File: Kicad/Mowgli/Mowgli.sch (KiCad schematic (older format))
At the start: 1 part

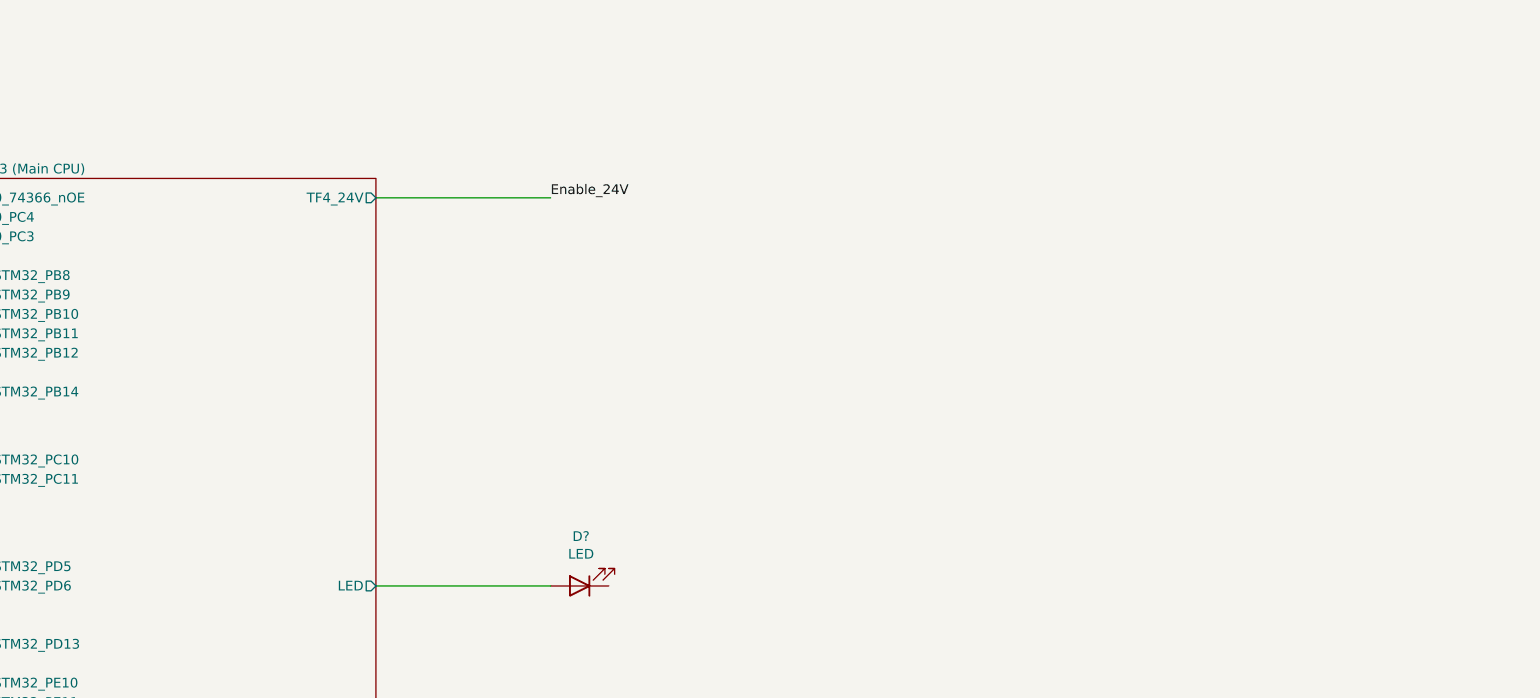
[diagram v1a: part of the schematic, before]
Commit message: updated Kicad with Charge/Battery Circuit
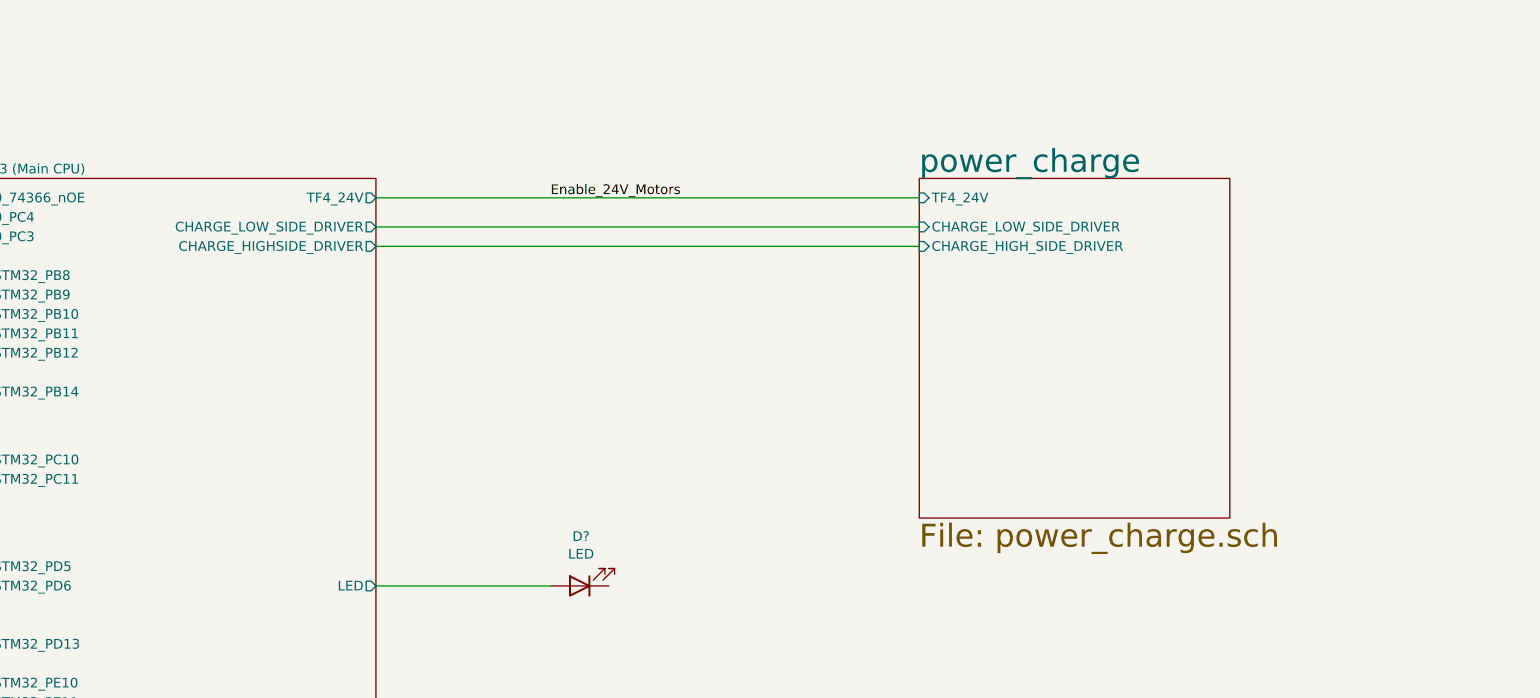
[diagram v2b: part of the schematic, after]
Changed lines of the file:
@@
 $Descr A3 16535 11693
 encoding utf-8
-Sheet 1 9
+Sheet 1 10
 Title "Project Mowgli"
 Date "2022-05-22"
@@
 F29 "ACCEL_SCL" O R 9500 6950 50
 F30 "ACCEL_SDA" O R 9500 7050 50
+F31 "CHARGE_LOW_SIDE_DRIVER" O R 9500 3100 50
+F32 "CHARGE_HIGHSIDE_DRIVER" O R 9500 3200 50
 $EndSheet
 Wire Wire Line
@@
 USART 3
 Text Label 10400 2950 0    50   ~ 0
-Enable_24V
-Wire Wire Line
-	9500 2950 10400 2950
+Enable_24V_Motors
 $Sheet
 S 5550 6950 850  1350
@@
 F30 "J18_Pin_8" I L 4200 6000 50
 $EndSheet
+$Sheet
+S 12300 2850 1600 1750
+U 628DB6FB
+F0 "power_charge" 118
+F1 "power_charge.sch" 118
+F2 "TF4_24V" I L 12300 2950 50
+F3 "CHARGE_LOW_SIDE_DRIVER" I L 12300 3100 50
+F4 "CHARGE_HIGH_SIDE_DRIVER" I L 12300 3200 50
+$EndSheet
+Wire Wire Line
+	9500 2950 12300 2950
+Wire Wire Line
+	12300 3100 9500 3100
+Wire Wire Line
+	9500 3200 12300 3200
 Wire Bus Line
 	6450 8750 6450 9050

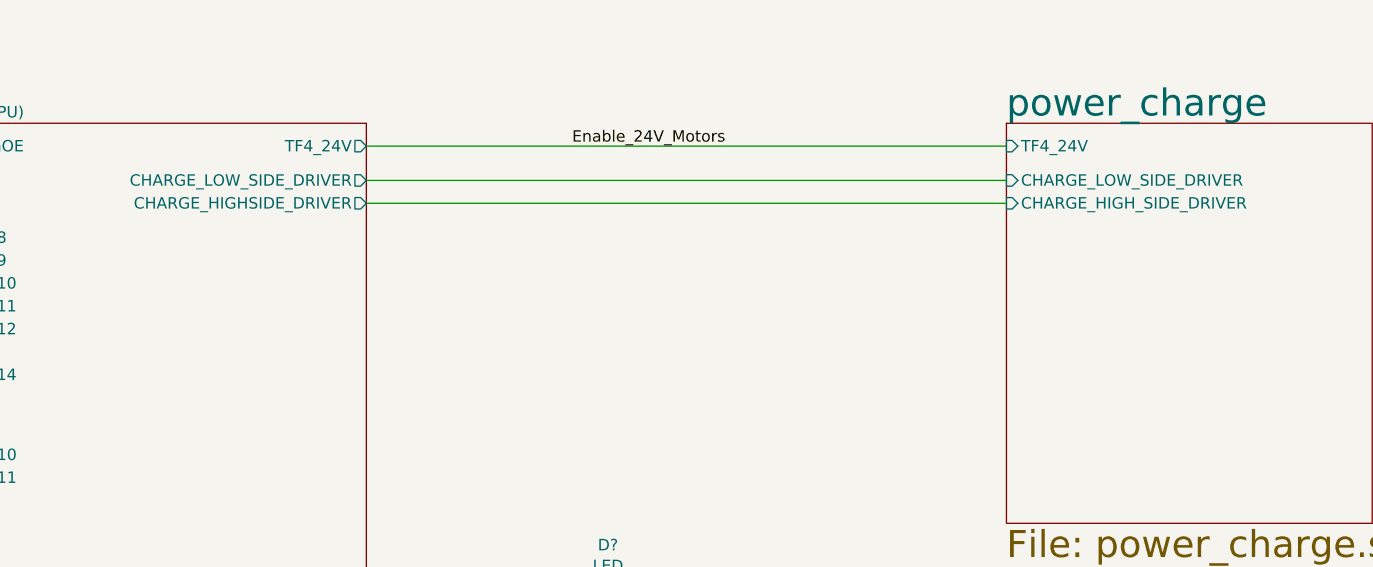
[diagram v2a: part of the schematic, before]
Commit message: added PA3 ADC input pin
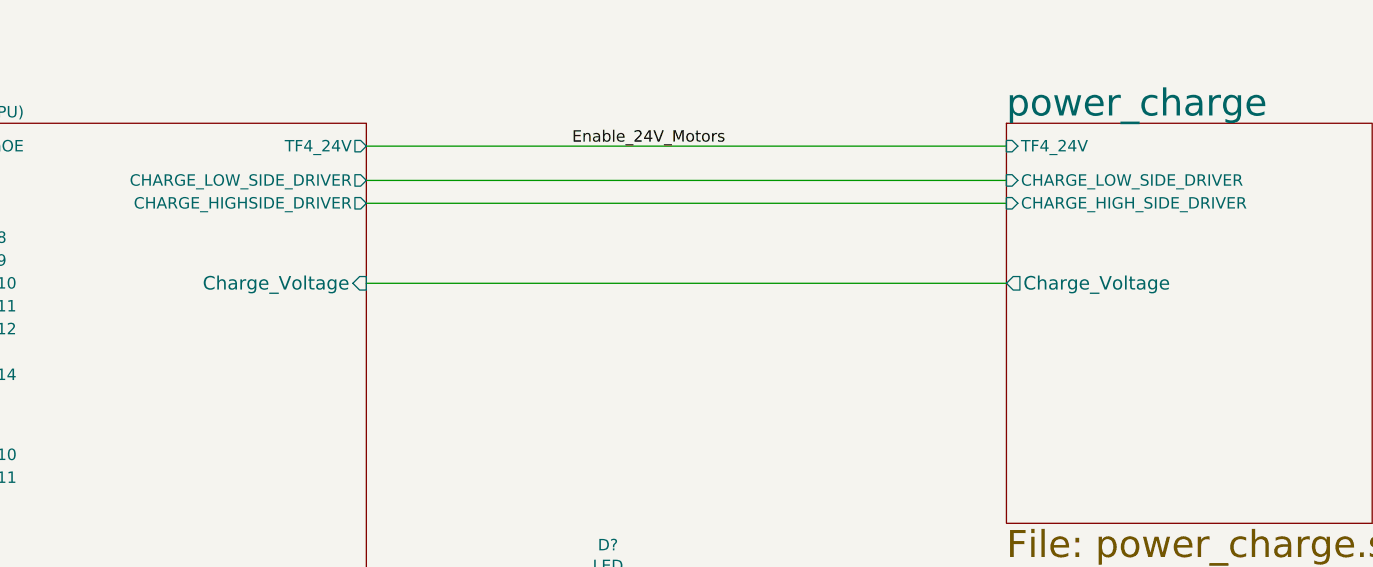
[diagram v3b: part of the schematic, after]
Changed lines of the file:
@@
 F31 "CHARGE_LOW_SIDE_DRIVER" O R 9500 3100 50
 F32 "CHARGE_HIGHSIDE_DRIVER" O R 9500 3200 50
+F33 "Charge_Voltage" I R 9500 3550 59
 $EndSheet
 Wire Wire Line
@@
 F3 "CHARGE_LOW_SIDE_DRIVER" I L 12300 3100 50
 F4 "CHARGE_HIGH_SIDE_DRIVER" I L 12300 3200 50
+F5 "Charge_Voltage" O L 12300 3550 59
 $EndSheet
 Wire Wire Line
@@
 Wire Wire Line
 	9500 3200 12300 3200
+Wire Wire Line
+	12300 3550 9500 3550
 Wire Bus Line
 	6450 8750 6450 9050

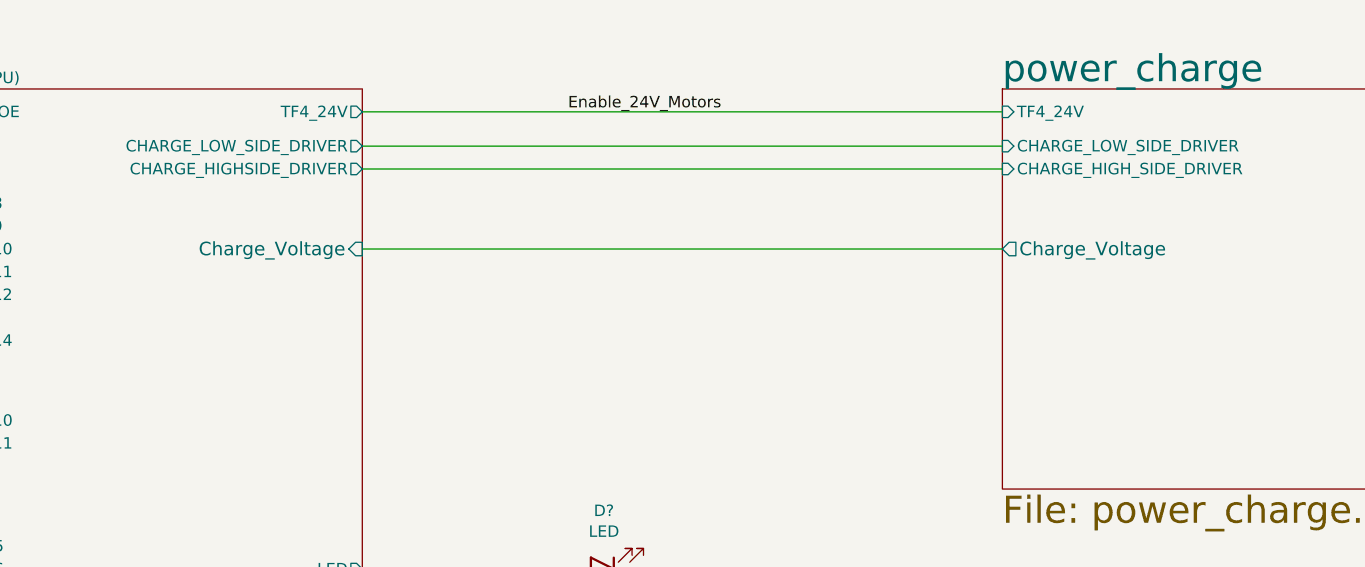
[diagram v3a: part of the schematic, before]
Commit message: PA2,PA3 are used for Charging and Battery Voltage monitoring - added stm32 code and updated KiCad
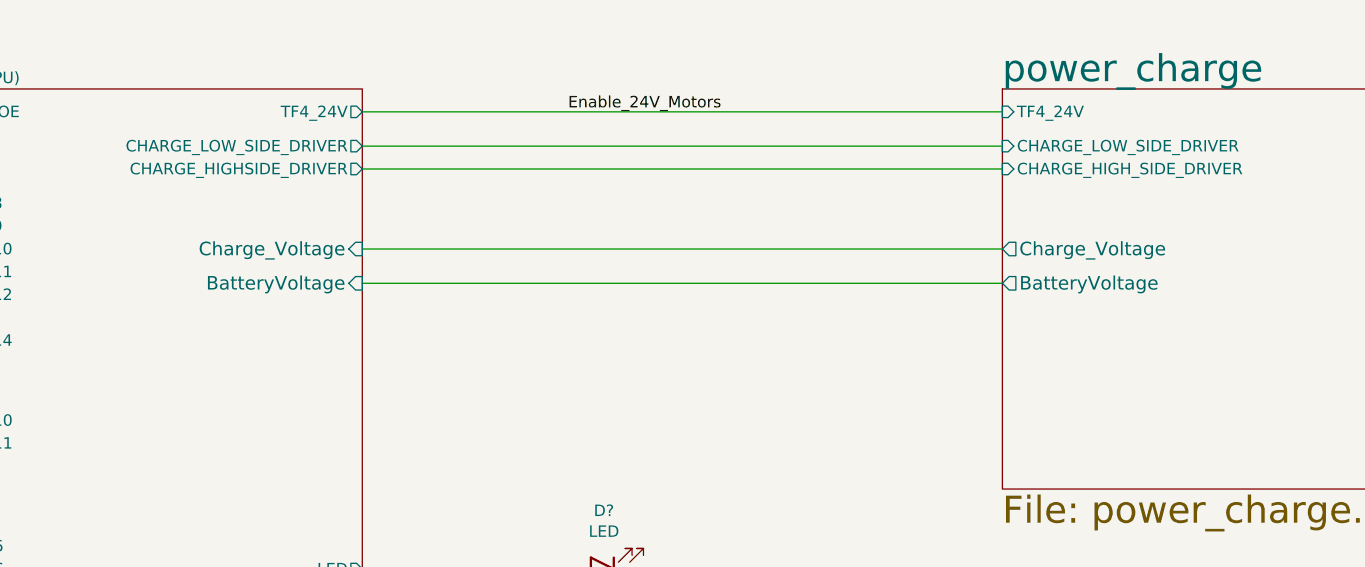
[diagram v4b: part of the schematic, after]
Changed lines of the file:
@@
 F32 "CHARGE_HIGHSIDE_DRIVER" O R 9500 3200 50
 F33 "Charge_Voltage" I R 9500 3550 59
+F34 "BatteryVoltage" I R 9500 3700 59
 $EndSheet
 Wire Wire Line
@@
 F4 "CHARGE_HIGH_SIDE_DRIVER" I L 12300 3200 50
 F5 "Charge_Voltage" O L 12300 3550 59
+F6 "BatteryVoltage" O L 12300 3700 59
 $EndSheet
 Wire Wire Line
@@
 Wire Wire Line
 	12300 3550 9500 3550
+Wire Wire Line
+	12300 3700 9500 3700
 Wire Bus Line
 	6450 8750 6450 9050

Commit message: updated kicad
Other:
- note added: "I2C1"
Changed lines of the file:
@@
 Wire Wire Line
 	12300 3700 9500 3700
+Text Notes 10800 7150 0    50   Italic 10
+I2C1
 Wire Bus Line
 	6450 8750 6450 9050

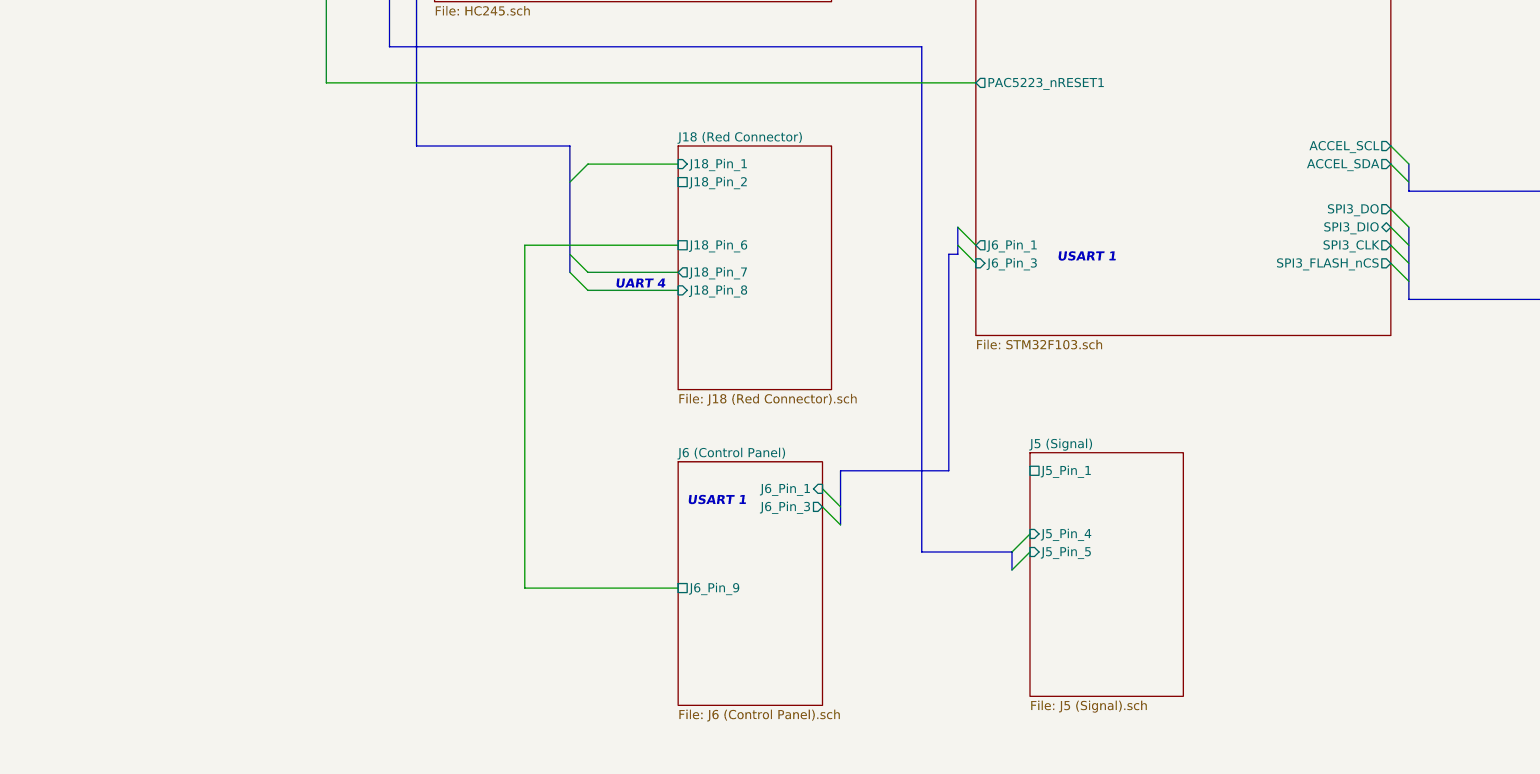
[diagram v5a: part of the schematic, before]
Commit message: added J18 SPI3 pins
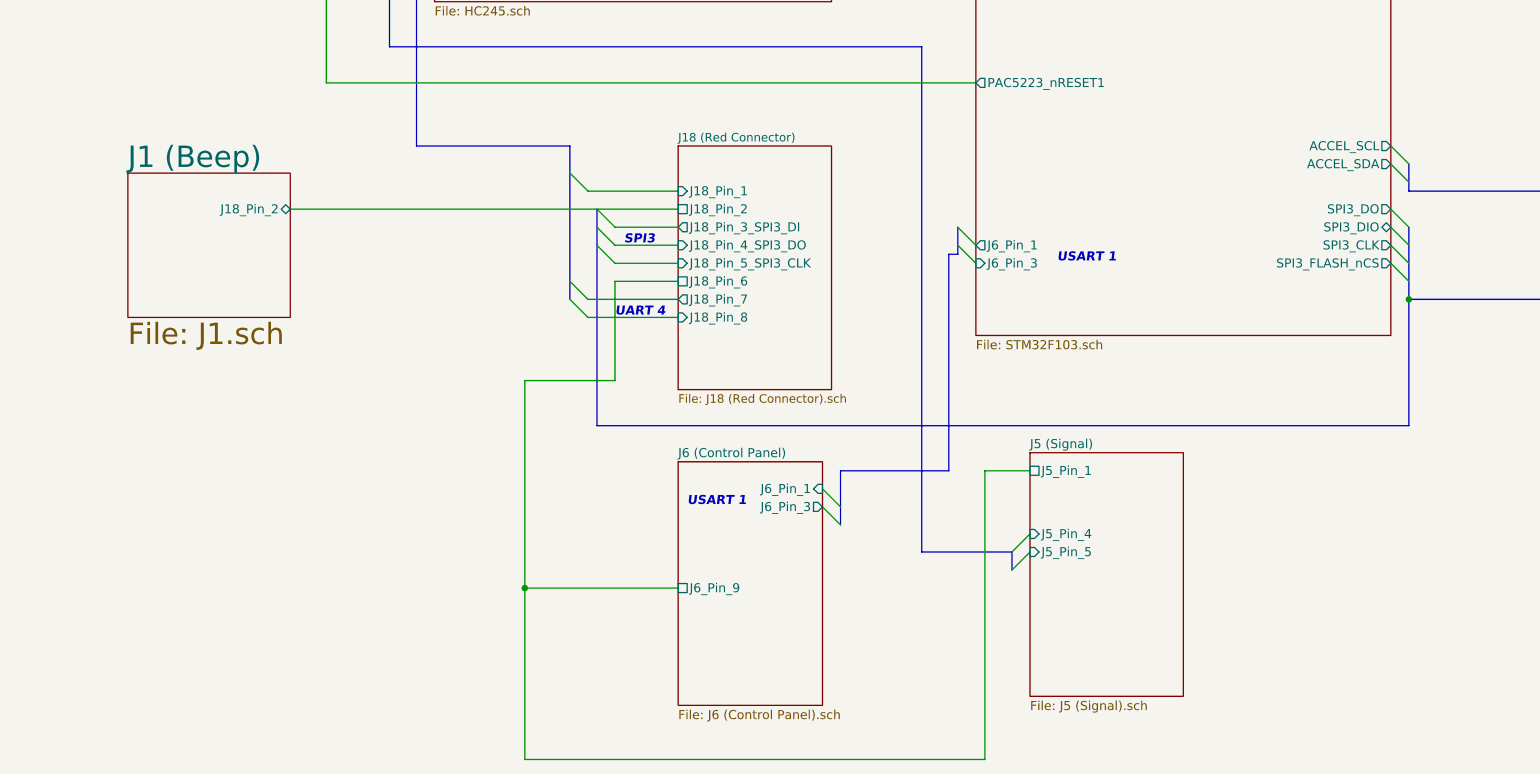
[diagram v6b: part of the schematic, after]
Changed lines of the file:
@@
 $Descr A3 16535 11693
 encoding utf-8
-Sheet 1 10
+Sheet 1 11
 Title "Project Mowgli"
 Date "2022-05-22"
@@
 S 5550 6950 850  1350
 U 62926FC8
-F0 "J18 (Red Connector)" 50
-F1 "J18 (Red Connector).sch" 50
-F2 "J18_Pin_1" I L 5550 7050 50
-F3 "J18_Pin_7" O L 5550 7650 50
-F4 "J18_Pin_8" I L 5550 7750 50
-F5 "J18_Pin_2" U L 5550 7150 50
-F6 "J18_Pin_6" U L 5550 7500 50
+F0 "J18 (Red Connector)" 47
+F1 "J18 (Red Connector).sch" 47
+F2 "J18_Pin_1" I L 5550 7200 50
+F3 "J18_Pin_7" O L 5550 7800 50
+F4 "J18_Pin_8" I L 5550 7900 50
+F5 "J18_Pin_2" U L 5550 7300 50
+F6 "J18_Pin_6" U L 5550 7700 50
+F7 "J18_Pin_5_SPI3_CLK" I L 5550 7600 50
+F8 "J18_Pin_4_SPI3_DO" I L 5550 7500 50
+F9 "J18_Pin_3_SPI3_DI" O L 5550 7400 50
 $EndSheet
 Entry Wire Line
@@
 	4100 6950 4950 6950
 Entry Wire Line
-	4950 7150 5050 7050
-Wire Wire Line
-	5550 7050 5050 7050
-Entry Wire Line
-	4950 7650 5050 7750
-Entry Wire Line
-	4950 7550 5050 7650
-Wire Wire Line
-	5550 7750 5050 7750
-Wire Wire Line
-	5050 7650 5550 7650
+	5050 7200 4950 7100
+Entry Wire Line
+	4950 7800 5050 7900
+Entry Wire Line
+	4950 7700 5050 7800
+Wire Wire Line
+	5550 7900 5050 7900
+Wire Wire Line
+	5050 7800 5550 7800
 Text Notes 4650 6000 0    50   Italic 10
 UART 4
-Text Notes 5200 7750 0    50   Italic 10
+Text Notes 5200 7900 0    50   Italic 10
 UART 4
 $Sheet
@@
 F4 "J6_Pin_3" O R 6350 8950 50
 $EndSheet
-Wire Wire Line
-	5550 7500 4700 7500
-Wire Wire Line
-	4700 7500 4700 9400
 Wire Wire Line
 	4700 9400 5550 9400
@@
 Text Notes 10800 7150 0    50   Italic 10
 I2C1
+Wire Wire Line
+	7500 8750 7250 8750
+Wire Wire Line
+	7250 8750 7250 10350
+Wire Wire Line
+	7250 10350 4700 10350
+Wire Wire Line
+	4700 10350 4700 9400
+Connection ~ 4700 9400
+Wire Wire Line
+	5550 7200 5050 7200
+Wire Wire Line
+	5550 7700 5200 7700
+Wire Wire Line
+	5200 7700 5200 8250
+Wire Wire Line
+	5200 8250 4700 8250
+Wire Wire Line
+	4700 8250 4700 9400
+Wire Bus Line
+	9600 7800 9600 8500
+Wire Bus Line
+	9600 8500 5100 8500
+Connection ~ 9600 7800
+Entry Wire Line
+	5100 7300 5200 7400
+Entry Wire Line
+	5100 7400 5200 7500
+Entry Wire Line
+	5100 7500 5200 7600
+Wire Wire Line
+	5550 7600 5200 7600
+Wire Wire Line
+	5200 7500 5550 7500
+Wire Wire Line
+	5550 7400 5200 7400
+Text Notes 5250 7500 0    50   Italic 10
+SPI3
+$Sheet
+S 2500 7100 900  800
+U 629B383F
+F0 "J1 (Beep)" 118
+F1 "J1.sch" 118
+F2 "J18_Pin_2" B R 3400 7300 50
+$EndSheet
 Wire Bus Line
 	6450 8750 6450 9050
@@
 	4100 5900 4100 6950
 Wire Bus Line
-	4950 6950 4950 7650
+	4950 6950 4950 7800
+Wire Wire Line
+	3400 7300 5550 7300
+Wire Bus Line
+	5100 7300 5100 8500
 Wire Bus Line
 	12200 7350 12200 7800
